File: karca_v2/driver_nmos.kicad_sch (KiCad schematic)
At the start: 10 parts, among them Q4 IRF3708

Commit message: revisions for V2.1
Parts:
- renumbered D9 to D18, D10 to D19, D11 to D20, F3 to F6, Q4 to Q7, R87 to R104, R88 to R105, R89 to R106, R90 to R107, TP45 to TP50

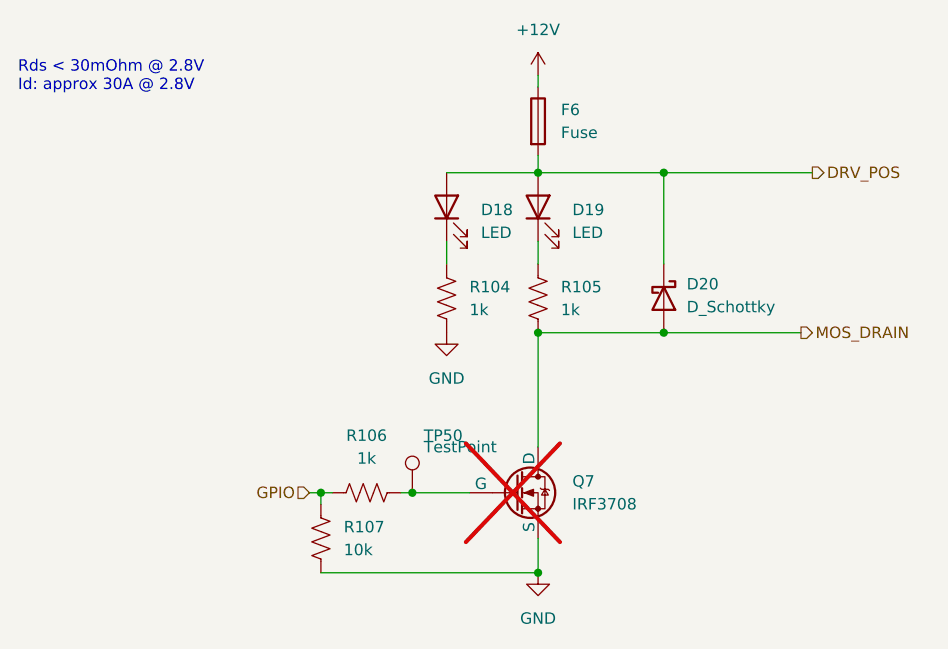
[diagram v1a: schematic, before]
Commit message: Replaced header with a smaller one, added silksreen labels, and removed secondary USB power source
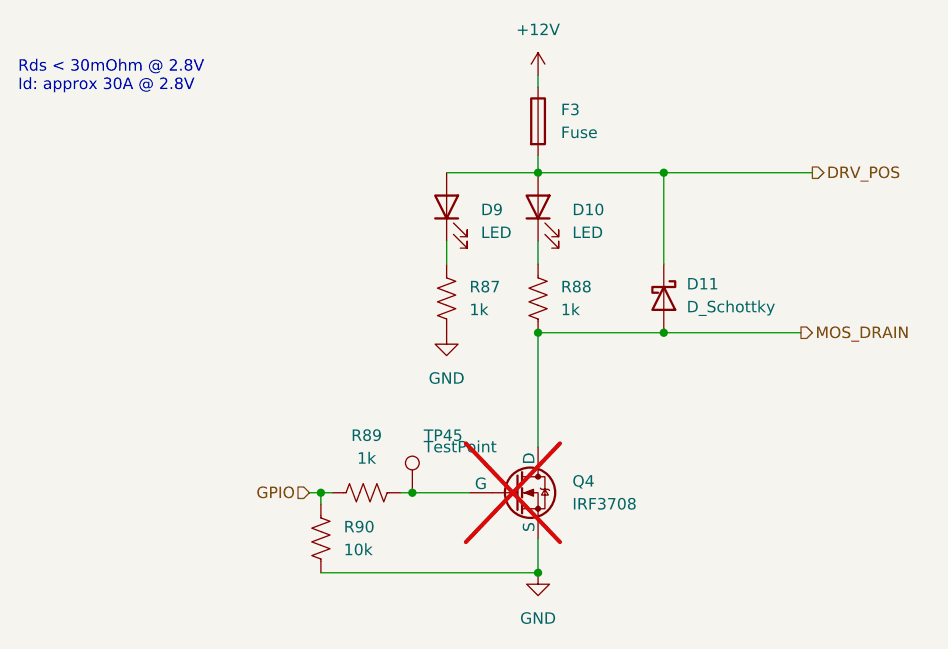
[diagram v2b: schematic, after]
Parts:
- renumbered D19 to D10, D20 to D11, D18 to D9, F6 to F3, Q7 to Q4, R104 to R87, R105 to R88, R106 to R89, R107 to R90, TP50 to TP45

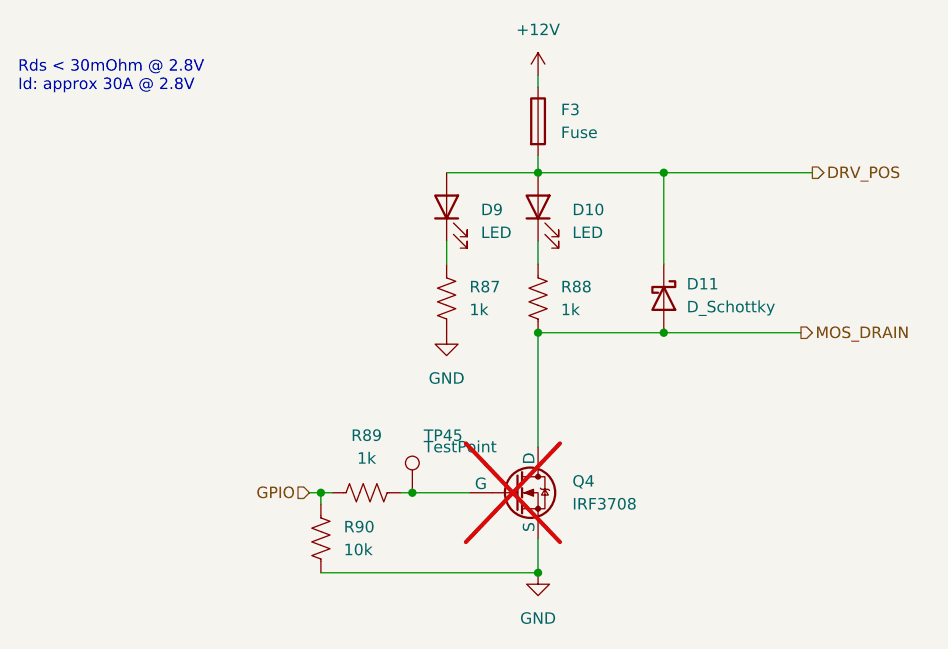
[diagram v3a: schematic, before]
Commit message: finished schematic for v2.1
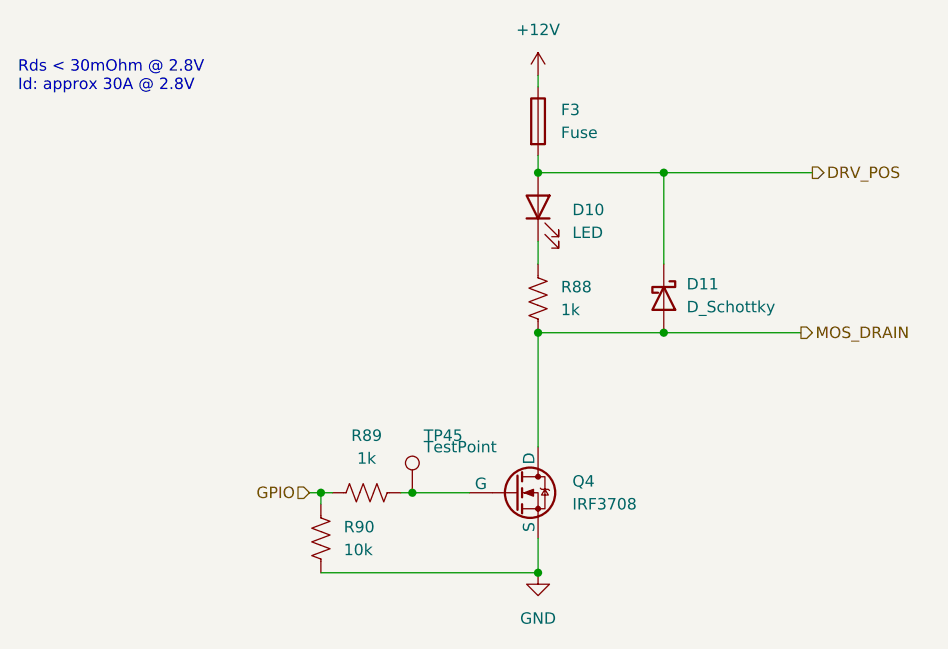
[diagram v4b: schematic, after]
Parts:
- removed D9: LED, LED_SMD:LED_1206_3216Metric, symbol Device:LED
- removed R87: 1k, Resistor_SMD:R_1206_3216Metric, symbol Device:R_US
- Q4: now fitted; now in the parts list

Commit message: swapped adcs
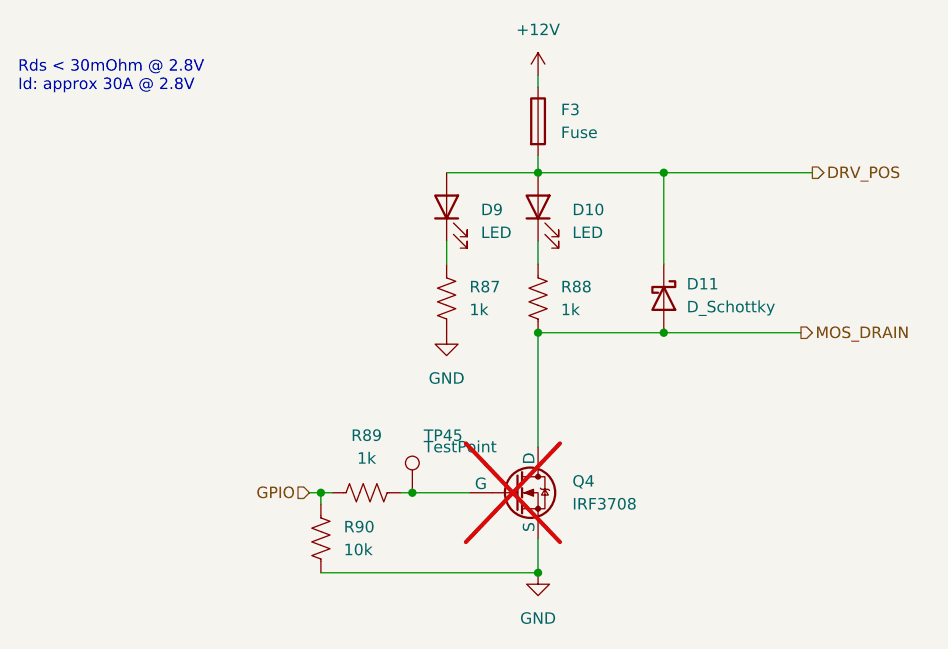
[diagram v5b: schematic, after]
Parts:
- added D9: LED, LED_SMD:LED_1206_3216Metric, symbol Device:LED
- added R87: 1k, Resistor_SMD:R_1206_3216Metric, symbol Device:R_US
- Q4: now not fitted; now left out of the parts list
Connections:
- net DRV_POS: now also D9.2 (A)
- net GND: now also R87.2
- new net: D9.1 (K), R87.1

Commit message: Swapped IRF3708 FETs for AO3400 for more compact package
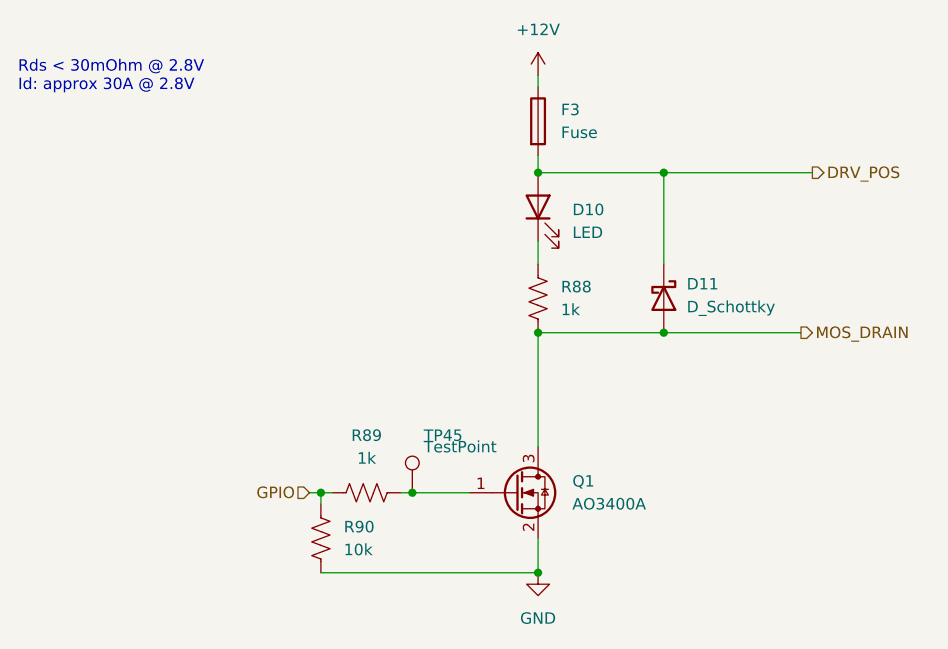
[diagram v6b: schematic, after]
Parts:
- removed D9: LED, LED_SMD:LED_1206_3216Metric, symbol Device:LED
- removed Q4: IRF3708, Package_TO_SOT_THT:TO-220-3_Vertical, symbol Simulation_SPICE:NMOS
- removed R87: 1k, Resistor_SMD:R_1206_3216Metric, symbol Device:R_US
- added Q1: AO3400A, Package_TO_SOT_SMD:SOT-23, symbol Transistor_FET:AO3400A
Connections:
- net GND: now also Q1.2 (S)
- net MOS_DRAIN: now also Q1.3 (D)
- net at R89.2, TP45.1: now also Q1.1 (G)

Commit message: final production version
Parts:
- D11: LCSC C727081 -> C7428238
- F3: LCSC C55996 -> C21010
- Q1: MPN (none) -> C20917
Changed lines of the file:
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@@
+			)
+		)
+		(property "MPN" "C20917"
+			(at 73.66 66.04 0)
+			(effects
+				(font
+					(size 1.27 1.27)
+				)
+				(hide yes)
 			)
 		)
@@
 			)
 		)
-		(property "LCSC" "C727081"
+		(property "LCSC" "C7428238"
 			(at 90.17 44.45 90)
 			(effects
@@
 			)
 		)
-		(property "LCSC" "C55996"
+		(property "LCSC" "C21010"
 			(at 76.2 24.765 0)
 			(effects
